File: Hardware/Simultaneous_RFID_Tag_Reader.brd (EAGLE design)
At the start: 77.5 x 53.3 mm, 40 parts, among them J2 FTDI, J3 JST, J4 U.FL, J5 Extra, J6 Screw Terminal, J7 GPIOs, U2 TXB0104, U3 ESD Diode, U4 Nano

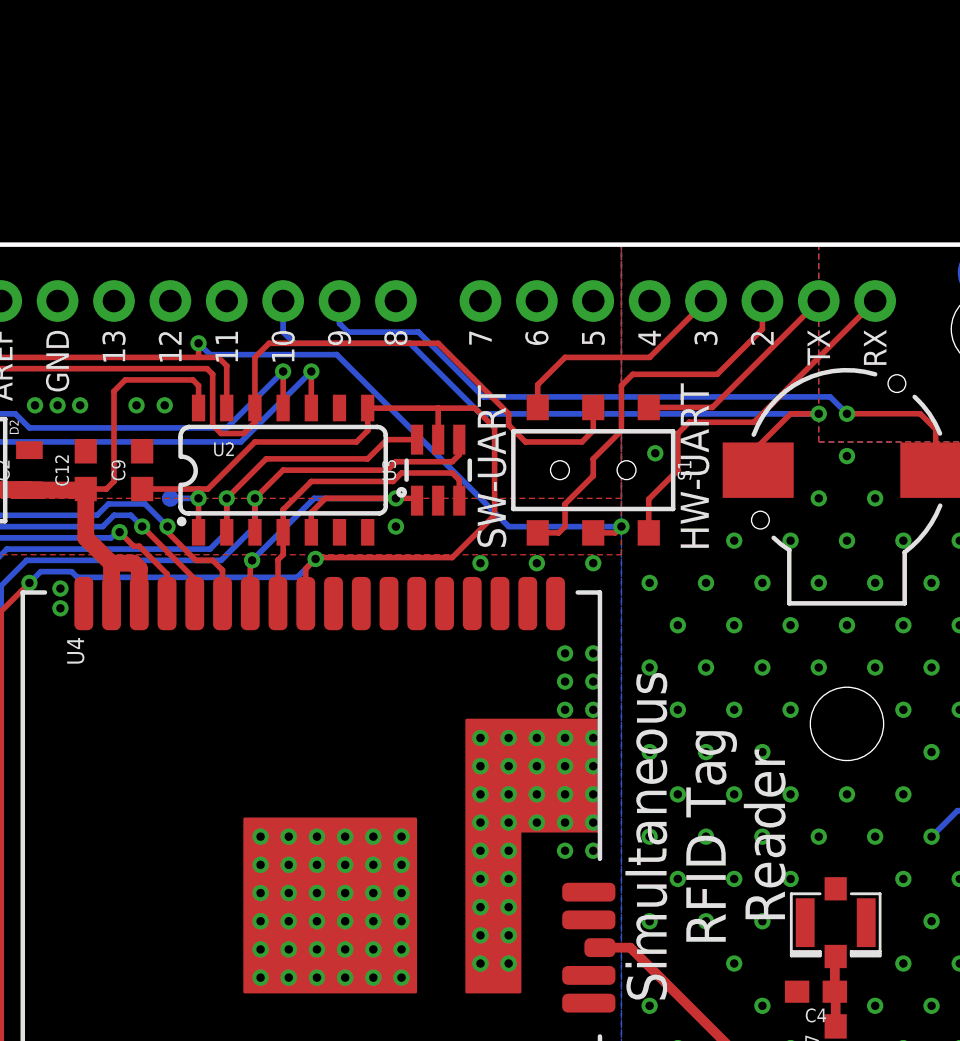
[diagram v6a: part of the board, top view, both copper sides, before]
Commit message: Added insulation to ISP and ground thermal. Added RF supressors to enable. Grounded half of buzzer.
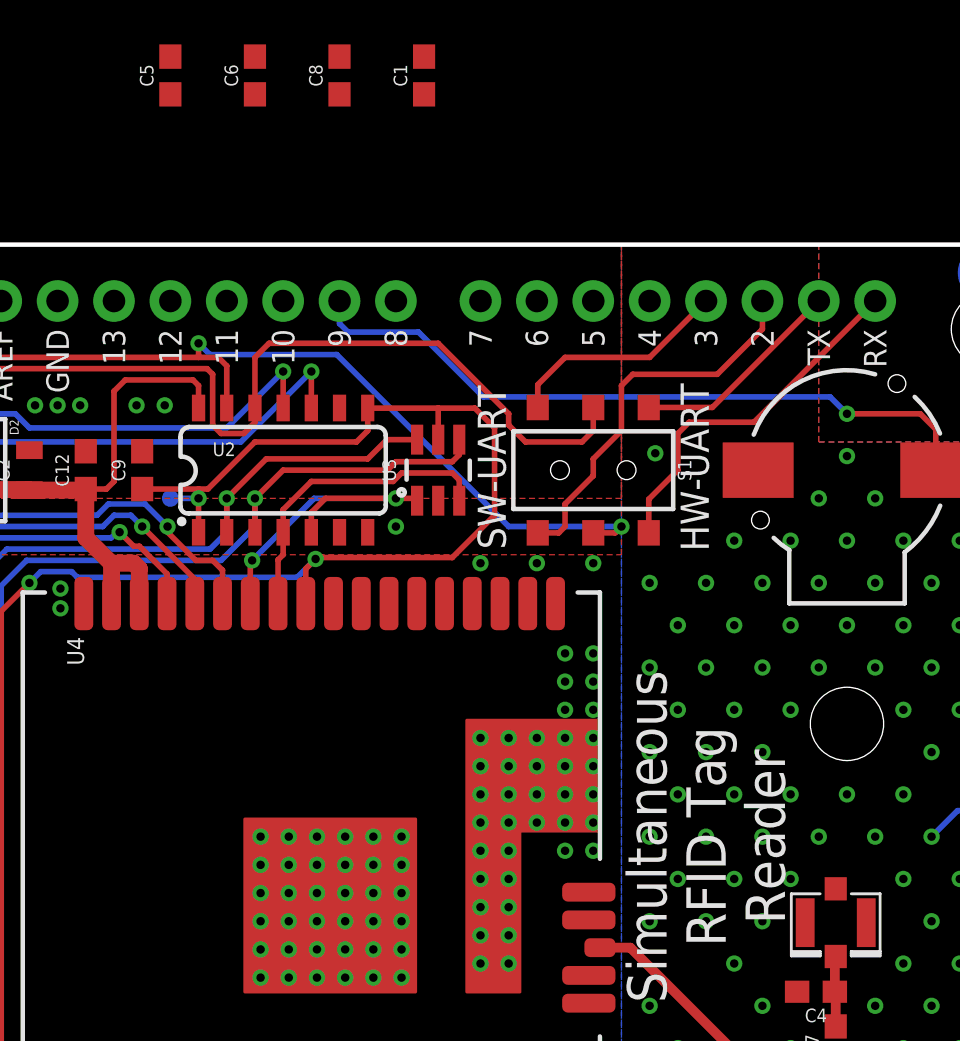
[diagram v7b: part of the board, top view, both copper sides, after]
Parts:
- added C1, C5, C6, C8: 47pF, SparkFun-Capacitors:0603
- moved FRAME1 6.48 mm to (0.00, -35.6)
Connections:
- removed net N$13: B1.D10, SG1.-
- net ENABLE-LV: now also C6.1
- net GND: now also C1.2, C5.2, C6.2, C8.2, SG1.-
- net GPIO1-LV: now also C8.1
- net RXI-LV: now also C5.1
- net TXO-LV: now also C1.1
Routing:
- net N$13: track 31.5 -> 0.00 mm, vias 1 -> 0

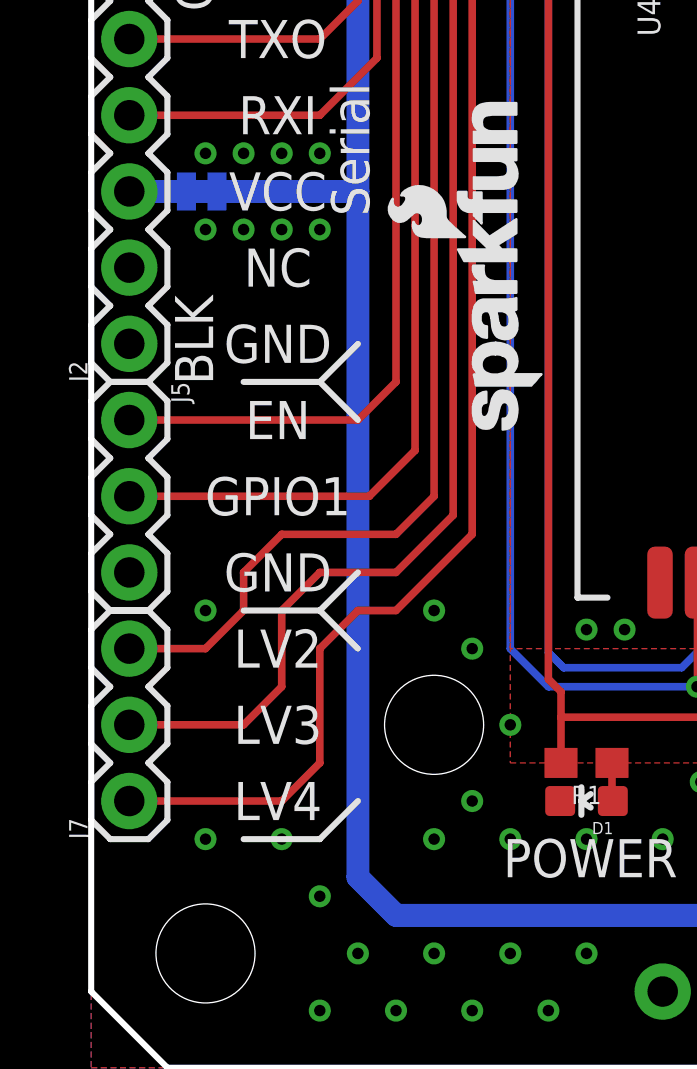
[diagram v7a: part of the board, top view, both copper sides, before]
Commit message: Adding pull up to enable pin
TXB0104 wants unused inputs to be in same state. This pull up does that
for the HV side.
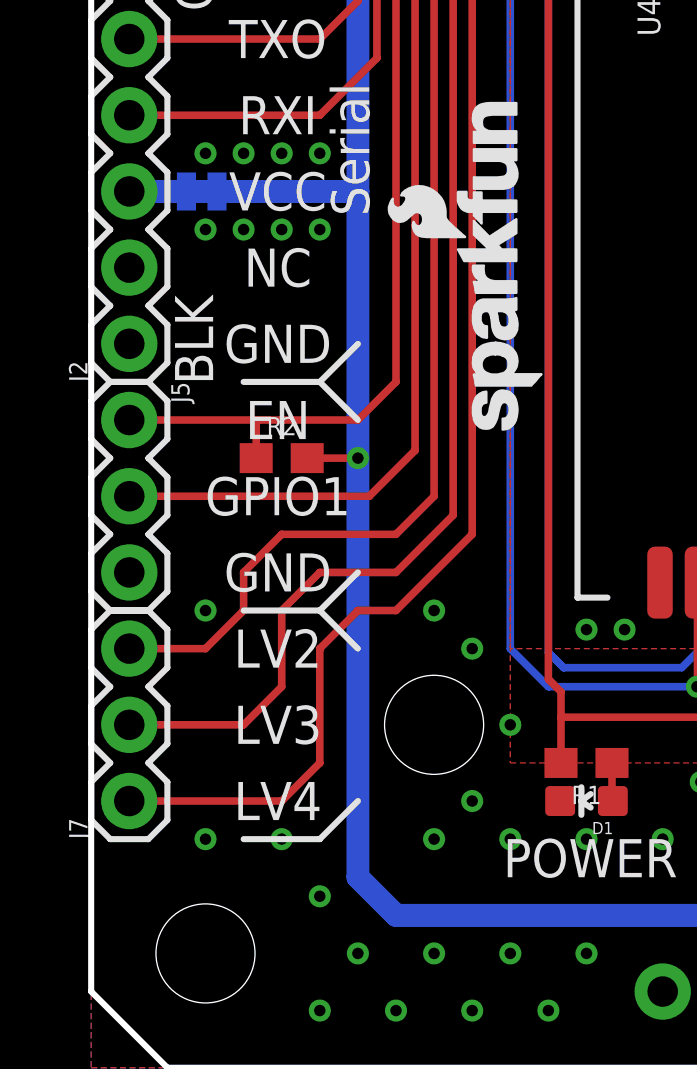
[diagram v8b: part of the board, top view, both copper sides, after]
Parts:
- added R2: 1k, SparkFun-Resistors:0603
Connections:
- net ENABLE: now also R2.1
- net VCC: now also R2.2
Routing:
- net VCC: track 93.0 -> 94.7 mm, vias 1 -> 2
- net ENABLE: track 52.3 -> 53.6 mm
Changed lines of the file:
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@@
 <layer number="47" name="Measures" color="7" fill="1" visible="no" active="yes"/>
 <layer number="48" name="Document" color="7" fill="1" visible="no" active="yes"/>
-<layer number="49" name="Reference" color="7" fill="1" visible="yes" active="yes"/>
+<layer number="49" name="Reference" color="7" fill="1" visible="no" active="yes"/>
 <layer number="50" name="dxf" color="7" fill="1" visible="no" active="no"/>
 <layer number="51" name="tDocu" color="6" fill="1" visible="yes" active="yes"/>
@@
 <attribute name="PROD_ID" value="CAP-08913" x="30.48" y="60.96" size="1.778" layer="27" font="vector" ratio="15" rot="R90" display="off"/>
 </element>
+<element name="R2" library="SparkFun-Resistors" package="0603" value="1k" x="6.35" y="20.32">
+<attribute name="PROD_ID" value="RES-07856" x="6.35" y="20.32" size="1.778" layer="27" font="vector" ratio="15" display="off"/>
+</element>
 </elements>
 <signals>
@@
 <contactref element="U2" pad="11"/>
 <contactref element="J5" pad="1"/>
-<wire x1="1.27" y1="21.59" x2="8.89" y2="21.59" width="0.254" layer="1"/>
+<wire x1="1.27" y1="21.59" x2="5.588" y2="21.59" width="0.254" layer="1"/>
 <via x="12.573" y="45.72" extent="1-16" drill="0.381"/>
 <via x="27.94" y="47.625" extent="1-16" drill="0.381"/>
+<wire x1="5.588" y1="21.59" x2="8.89" y2="21.59" width="0.254" layer="1"/>
 <wire x1="27.94" y1="47.625" x2="27.94" y2="45.98" width="0.254" layer="1"/>
 <wire x1="25.4" y1="45.085" x2="27.94" y2="47.625" width="0.254" layer="16"/>
@@
 <wire x1="12.573" y1="45.72" x2="11.43" y2="45.72" width="0.254" layer="1"/>
 <wire x1="11.43" y1="45.72" x2="10.16" y2="44.45" width="0.254" layer="1"/>
+<contactref element="R2" pad="1"/>
+<wire x1="5.5" y1="20.32" x2="5.5" y2="21.502" width="0.254" layer="1"/>
+<wire x1="5.5" y1="21.502" x2="5.588" y2="21.59" width="0.254" layer="1"/>
 </signal>
 <signal name="GPIO1">
@@
 <wire x1="20.21" y1="37.17" x2="20.21" y2="38.972" width="0.762" layer="1"/>
 <wire x1="21.46" y1="37.17" x2="21.46" y2="38.738" width="0.762" layer="1"/>
-<wire x1="8.89" y1="6.35" x2="8.89" y2="29.21" width="0.762" layer="16"/>
+<wire x1="8.89" y1="6.35" x2="8.89" y2="20.32" width="0.762" layer="16"/>
+<contactref element="R2" pad="2"/>
+<wire x1="8.89" y1="20.32" x2="8.89" y2="29.21" width="0.762" layer="16"/>
+<wire x1="7.2" y1="20.32" x2="8.89" y2="20.32" width="0.254" layer="1"/>
+<via x="8.89" y="20.32" extent="1-16" drill="0.381"/>
 </signal>
 <signal name="ANT3">
